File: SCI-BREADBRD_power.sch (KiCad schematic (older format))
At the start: 3 parts, among them SW1 DPDT, U1 SN74LVC1G08DBV

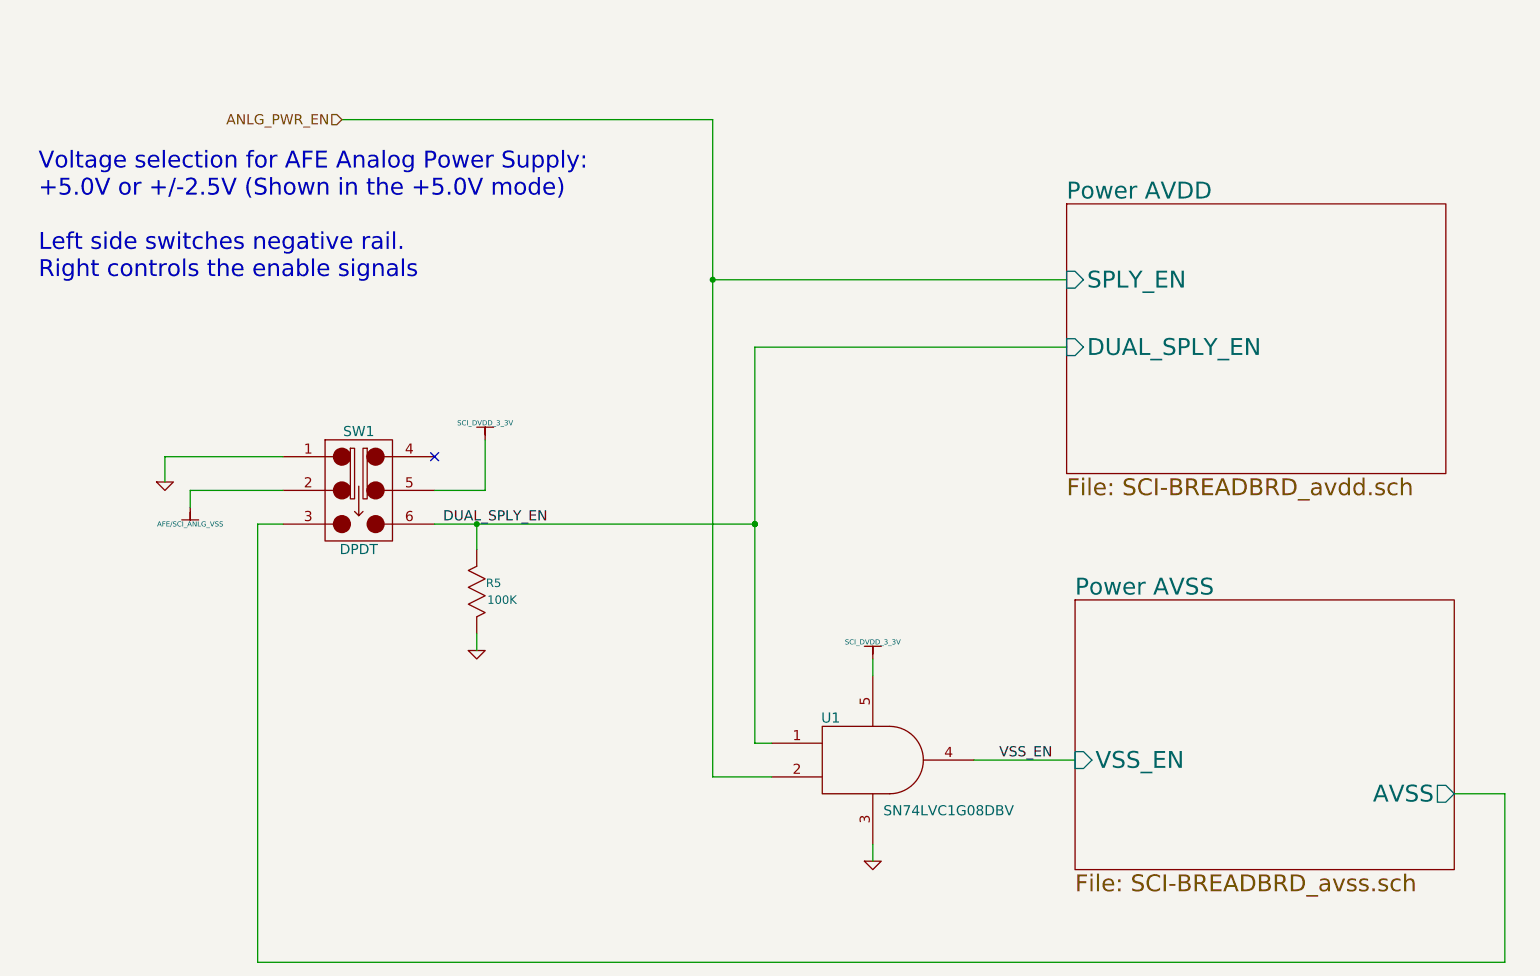
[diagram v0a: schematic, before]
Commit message: Completed ERC. Added some power flags and fixed mis-connected pins.
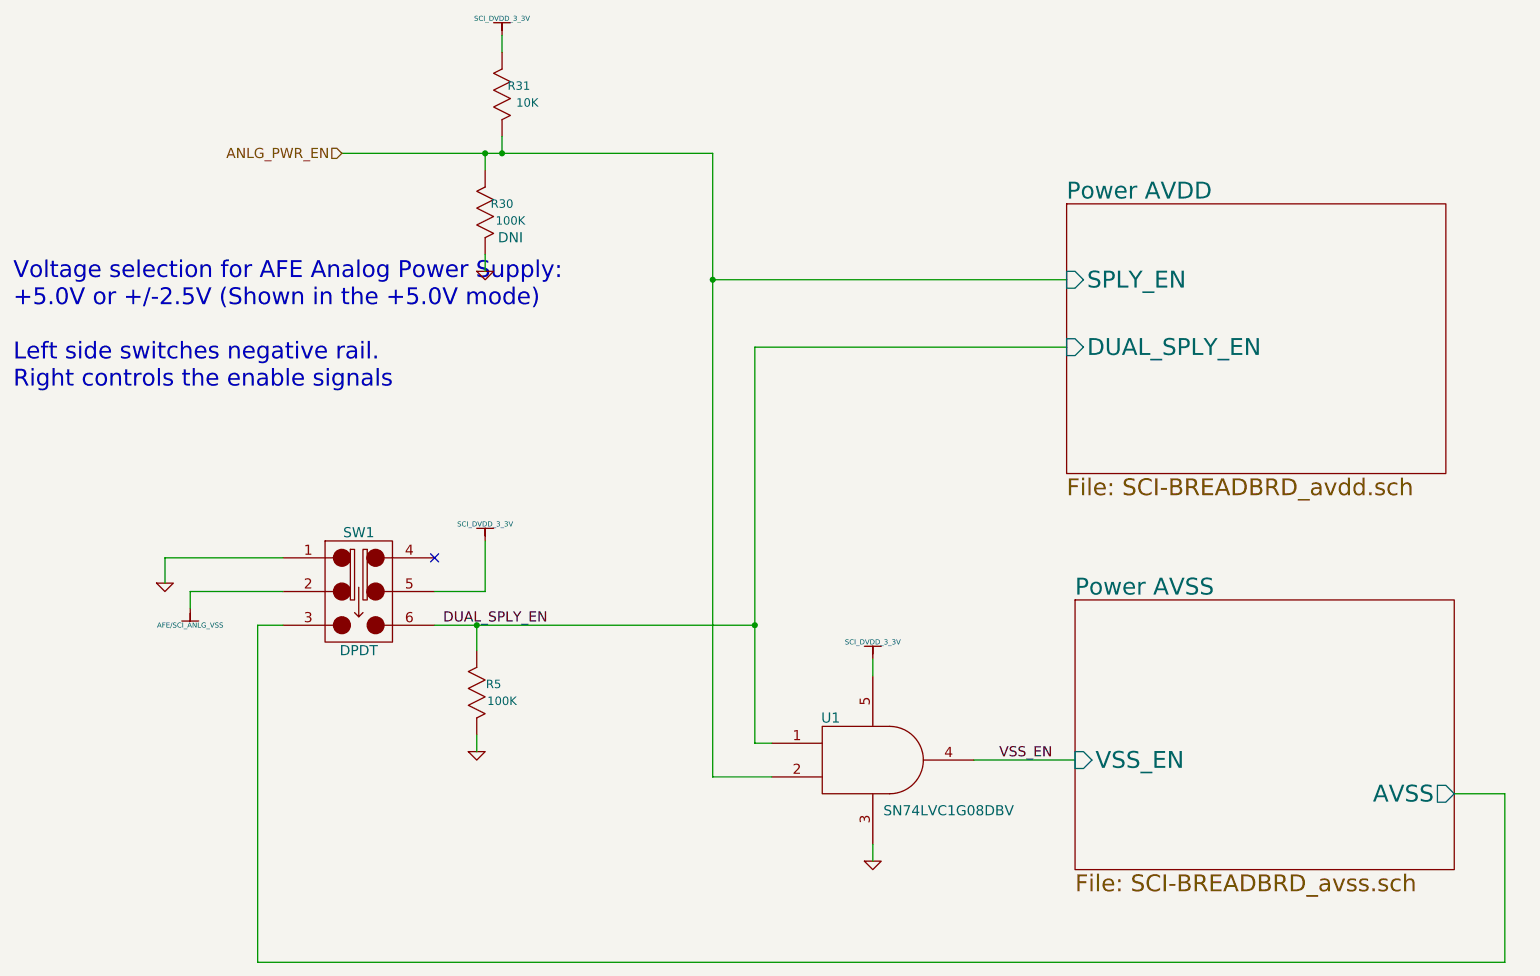
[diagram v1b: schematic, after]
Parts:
- added R30: 100K, 0402, symbol R_US
- added R31: 10K, 0402, symbol R_US
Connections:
- net ANLG_PWR_EN: now also R30.2 (B), R31.1 (A)
- net GND: now also R30.1 (A)
- net SCI_DVDD_3_3V: now also R31.2 (B)
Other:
- moved on the sheet: R5, SW1
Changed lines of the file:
@@
-EESchema Schematic File Version 2  date Fri 27 Apr 2012 09:11:54 AM EDT
+EESchema Schematic File Version 2  date Fri 27 Apr 2012 11:11:24 AM EDT
 LIBS:custom_transistors
 LIBS:TI_custom
@@
 L DPDT SW1
 U 1 1 4F8CA839
-P 2900 3400
-F 0 "SW1" H 2900 3750 60  0000 C CNN
-F 1 "DPDT" H 2900 3050 60  0000 C CNN
-F 2 "CK_DPDT_SMT" H 2900 3400 60  0001 C CNN
-F 4 "C&K Components" H 2900 3400 60  0001 C CNN "Manufacturer"
-F 5 "JS202011SCQN" H 2900 3400 60  0001 C CNN "Part Number"
-F 6 "SWITCH SLIDE DPDT 6VDC 0.3A SMT" H 2900 3400 60  0001 C CNN "Description"
-	1    2900 3400
+P 2900 4000
+F 0 "SW1" H 2900 4350 60  0000 C CNN
+F 1 "DPDT" H 2900 3650 60  0000 C CNN
+F 2 "CK_DPDT_SMT" H 2900 4000 60  0001 C CNN
+F 4 "C&K Components" H 2900 4000 60  0001 C CNN "Manufacturer"
+F 5 "JS202011SCQN" H 2900 4000 60  0001 C CNN "Part Number"
+F 6 "SWITCH SLIDE DPDT 6VDC 0.3A SMT" H 2900 4000 60  0001 C CNN "Description"
+	1    2900 4000
 	1    0    0    -1
 $EndComp
@@
 $EndComp
 $Comp
-L AFE/SCI_ANLG_VSS #PWR040
+L AFE/SCI_ANLG_VSS #PWR042
 U 1 1 4F9A14F6
-P 1900 3500
-F 0 "#PWR040" H 1900 3400 30  0001 C CNN
-F 1 "AFE/SCI_ANLG_VSS" H 1900 3400 30  0000 C CNN
-	1    1900 3500
-	1    0    0    -1
-$EndComp
-$Comp
-L GND #PWR041
+P 1900 4100
+F 0 "#PWR042" H 1900 4000 30  0001 C CNN
+F 1 "AFE/SCI_ANLG_VSS" H 1900 4000 30  0000 C CNN
+	1    1900 4100
+	1    0    0    -1
+$EndComp
+$Comp
+L GND #PWR043
 U 1 1 4F9A1627
-P 1750 3350
-F 0 "#PWR041" H 1750 3350 30  0001 C CNN
-F 1 "GND" H 1750 3280 30  0001 C CNN
-	1    1750 3350
-	1    0    0    -1
-$EndComp
-$Comp
-L SCI_DVDD_3_3V #PWR042
+P 1750 3950
+F 0 "#PWR043" H 1750 3950 30  0001 C CNN
+F 1 "GND" H 1750 3880 30  0001 C CNN
+	1    1750 3950
+	1    0    0    -1
+$EndComp
+$Comp
+L SCI_DVDD_3_3V #PWR044
 U 1 1 4F9A18A3
-P 3650 3100
-F 0 "#PWR042" H 3650 3200 30  0001 C CNN
-F 1 "SCI_DVDD_3_3V" H 3650 3200 30  0000 C CNN
-	1    3650 3100
-	1    0    0    -1
-$EndComp
-NoConn ~ 3350 3200
-Text Label 3400 3600 0    60   ~ 0
+P 3650 3700
+F 0 "#PWR044" H 3650 3800 30  0001 C CNN
+F 1 "SCI_DVDD_3_3V" H 3650 3800 30  0000 C CNN
+	1    3650 3700
+	1    0    0    -1
+$EndComp
+NoConn ~ 3350 3800
+Text Label 3400 4200 0    60   ~ 0
 DUAL_SPLY_EN
 $Comp
-L SCI_DVDD_3_3V #PWR043
+L SCI_DVDD_3_3V #PWR045
 U 1 1 4F9A1DFD
 P 5950 4400
-F 0 "#PWR043" H 5950 4500 30  0001 C CNN
+F 0 "#PWR045" H 5950 4500 30  0001 C CNN
 F 1 "SCI_DVDD_3_3V" H 5950 4500 30  0000 C CNN
 	1    5950 4400
@@
 $EndComp
 $Comp
-L GND #PWR044
+L GND #PWR046
 U 1 1 4F9A1F73
 P 5950 5600
-F 0 "#PWR044" H 5950 5600 30  0001 C CNN
+F 0 "#PWR046" H 5950 5600 30  0001 C CNN
 F 1 "GND" H 5950 5530 30  0001 C CNN
 	1    5950 5600
@@
 F3 "VSS_EN" I L 7150 5000 100
 $EndSheet
-Text HLabel 2800 1200 0    60   Input ~ 0
+Text HLabel 2800 1400 0    60   Input ~ 0
 ANLG_PWR_EN
 $Comp
 L R_US R5
 U 1 1 4F9A4A29
-P 3600 4000
-F 0 "R5" V 3650 3900 50  0000 C CNN
-F 1 "100K" V 3550 3850 50  0000 C CNN
-F 2 "0402" H 3600 4000 60  0001 C CNN
-F 4 "Panasonic - ECG" H 3600 4000 60  0001 C CNN "Manufacturer"
-F 5 "ERJ-2GEJ104X" H 3600 4000 60  0001 C CNN "Part Number"
-F 6 "RES 100K OHM 1/10W 5% 0402 SMD" H 3600 4000 60  0001 C CNN "Description"
-	1    3600 4000
+P 3600 4600
+F 0 "R5" V 3650 4500 50  0000 C CNN
+F 1 "100K" V 3550 4450 50  0000 C CNN
+F 2 "0402" H 3600 4600 60  0001 C CNN
+F 4 "Panasonic - ECG" H 3600 4600 60  0001 C CNN "Manufacturer"
+F 5 "ERJ-2GEJ104X" H 3600 4600 60  0001 C CNN "Part Number"
+F 6 "RES 100K OHM 1/10W 5% 0402 SMD" H 3600 4600 60  0001 C CNN "Description"
+	1    3600 4600
 	0    -1   -1   0
 $EndComp
 $Comp
-L GND #PWR045
+L GND #PWR047
 U 1 1 4F9A4A85
-P 3600 4350
-F 0 "#PWR045" H 3600 4350 30  0001 C CNN
-F 1 "GND" H 3600 4280 30  0001 C CNN
-	1    3600 4350
-	1    0    0    -1
-$EndComp
-Text Notes 1000 2150 0    100  ~ 0
+P 3600 4950
+F 0 "#PWR047" H 3600 4950 30  0001 C CNN
+F 1 "GND" H 3600 4880 30  0001 C CNN
+	1    3600 4950
+	1    0    0    -1
+$EndComp
+Text Notes 850  2800 0    100  ~ 0
 Voltage selection for AFE Analog Power Supply:\n+5.0V or +/-2.5V (Shown in the +5.0V mode)\n\nLeft side switches negative rail.\nRight controls the enable signals
-Wire Wire Line
-	1900 3500 1900 3400
-Wire Wire Line
-	1900 3400 2450 3400
-Wire Wire Line
-	1750 3350 1750 3200
-Wire Wire Line
-	1750 3200 2450 3200
-Wire Wire Line
-	2450 3600 2300 3600
-Wire Wire Line
-	2300 3600 2300 6200
-Wire Wire Line
-	3350 3400 3650 3400
-Wire Wire Line
-	3650 3400 3650 3100
-Wire Wire Line
-	3350 3600 5250 3600
+$Comp
+L R_US R30
+U 1 1 4F9AB46A
+P 3650 1750
+F 0 "R30" V 3700 1650 50  0000 C CNN
+F 1 "100K" V 3600 1600 50  0000 C CNN
+F 2 "0402" H 3650 1750 60  0001 C CNN
+F 4 "Panasonic - ECG" H 3650 1750 60  0001 C CNN "Manufacturer"
+F 5 "ERJ-2GEJ104X" H 3650 1750 60  0001 C CNN "Part Number"
+F 6 "RES 100K OHM 1/10W 5% 0402 SMD" H 3650 1750 60  0001 C CNN "Description"
+F 7 "DNI" V 3500 1600 60  0000 C CNN "Note"
+	1    3650 1750
+	0    -1   -1   0
+$EndComp
+$Comp
+L GND #PWR048
+U 1 1 4F9AB470
+P 3650 2100
+F 0 "#PWR048" H 3650 2100 30  0001 C CNN
+F 1 "GND" H 3650 2030 30  0001 C CNN
+	1    3650 2100
+	1    0    0    -1
+$EndComp
+$Comp
+L R_US R31
+U 1 1 4F9AB66E
+P 3750 1050
+F 0 "R31" V 3800 950 50  0000 C CNN
+F 1 "10K" V 3700 900 50  0000 C CNN
+F 2 "0402" H 3750 1050 60  0001 C CNN
+F 4 "Panasonic - ECG" H 3750 1050 60  0001 C CNN "Manufacturer"
+F 5 "ERJ-2GEJ103X" H 3750 1050 60  0001 C CNN "Part Number"
+F 6 "RES 10K OHM 1/10W 5% 0402 SMD" H 3750 1050 60  0001 C CNN "Description"
+F 7 "DNI" H 3750 1050 60  0001 C CNN "Note"
+	1    3750 1050
+	0    -1   -1   0
+$EndComp
+$Comp
+L SCI_DVDD_3_3V #PWR049
+U 1 1 4F9AB960
+P 3750 700
+F 0 "#PWR049" H 3750 800 30  0001 C CNN
+F 1 "SCI_DVDD_3_3V" H 3750 800 30  0000 C CNN
+	1    3750 700
+	1    0    0    -1
+$EndComp
+Wire Wire Line
+	1900 4100 1900 4000
+Wire Wire Line
+	1900 4000 2450 4000
+Wire Wire Line
+	1750 3950 1750 3800
+Wire Wire Line
+	1750 3800 2450 3800
+Wire Wire Line
+	2450 4200 2300 4200
+Wire Wire Line
+	2300 4200 2300 6200
+Wire Wire Line
+	3350 4000 3650 4000
+Wire Wire Line
+	3650 4000 3650 3700
 Wire Wire Line
 	5950 4400 5950 4500
@@
 	5250 2550 7100 2550
 Wire Wire Line
-	2800 1200 5000 1200
-Wire Wire Line
-	5000 1200 5000 5100
+	2800 1400 5000 1400
+Wire Wire Line
+	5000 1400 5000 5100
 Wire Wire Line
 	5000 5100 5350 5100
@@
 Connection ~ 5000 2150
 Wire Wire Line
-	3600 3750 3600 3600
-Connection ~ 3600 3600
-Wire Wire Line
-	3600 4350 3600 4250
-Connection ~ 5250 3600
-Connection ~ 5250 3600
+	3600 4350 3600 4200
+Connection ~ 3600 4200
+Wire Wire Line
+	3600 4950 3600 4850
+Wire Wire Line
+	3650 2100 3650 2000
+Wire Wire Line
+	3650 1500 3650 1400
+Connection ~ 3650 1400
+Wire Wire Line
+	3750 1300 3750 1400
+Connection ~ 3750 1400
+Wire Wire Line
+	3750 700  3750 800
+Wire Wire Line
+	3350 4200 5250 4200
+Connection ~ 5250 4200
 $EndSCHEMATC

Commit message: Fixed component properties to make the BOM look nicer
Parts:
- R31: Note DNI -> (none)
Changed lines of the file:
@@
-EESchema Schematic File Version 2  date Fri 27 Apr 2012 11:11:24 AM EDT
+EESchema Schematic File Version 2  date Fri 27 Apr 2012 12:38:29 PM EDT
 LIBS:custom_transistors
 LIBS:TI_custom
@@
 F 5 "ERJ-2GEJ103X" H 3750 1050 60  0001 C CNN "Part Number"
 F 6 "RES 10K OHM 1/10W 5% 0402 SMD" H 3750 1050 60  0001 C CNN "Description"
-F 7 "DNI" H 3750 1050 60  0001 C CNN "Note"
 	1    3750 1050
 	0    -1   -1   0
